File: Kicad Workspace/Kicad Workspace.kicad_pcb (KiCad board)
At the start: 2 copper layers, 105 parts, among them U2 PCM1863DBT, U4 TMUX1574PW, U6 TLV76733DRVx, U7 LM5017MR, U8 LT3042xMSE, U9 STM32G030C8Tx, Y1 Crystal

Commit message: project update
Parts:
- added J1: NMJ4HFD2, Connector_Audio:Jack_6.35mm_Neutrik_NMJ4HFD2_Horizontal, F.Cu at (235.5, 44.0)
- added J2: NMJ4HFD2, Connector_Audio:Jack_6.35mm_Neutrik_NMJ4HFD2_Horizontal, F.Cu at (235.5, 65.3)
- added J3: NMJ6HFD2, Connector_Audio:Jack_6.35mm_Neutrik_NMJ6HFD2_Horizontal, F.Cu at (235.5, 86.6)
- added J4: NMJ4HFD2, Connector_Audio:Jack_6.35mm_Neutrik_NMJ4HFD2_Horizontal, F.Cu at (235.5, 107.9)
- added U1: ~, FootPrints:FSC-BT1058, F.Cu at (64.0, 157.5)
- moved C22 24.3 mm to (129.3, 163.2)
- moved C23 24.3 mm to (129.3, 168.4)
- moved C13 24.3 mm to (121.8, 159.5)
- moved C14 24.3 mm to (123.8, 160.0)
- moved C15 24.3 mm to (123.8, 162.5)
- moved C16 24.3 mm to (121.8, 162.9)
- moved C19 24.3 mm to (121.8, 155.7)
- moved U2 24.3 mm to (135.5, 164.0)
- moved Y1 24.3 mm to (129.0, 165.8)
- moved C17 24.3 mm to (131.7, 169.2)
- moved C18 24.3 mm to (132.2, 171.1)
- moved U4 5.84 mm to (108.0, 46.5)

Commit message: feat: routing work in progress
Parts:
- added J5: L+, Connector_Wire:SolderWirePad_1x01_SMD_2x4mm, F.Cu at (201.5, 20.9)
- added J6: L-, Connector_Wire:SolderWirePad_1x01_SMD_2x4mm, F.Cu at (205.1, 20.9)
- added J7: R+, Connector_Wire:SolderWirePad_1x01_SMD_2x4mm, F.Cu at (208.6, 20.9)
- added J8: R-, Connector_Wire:SolderWirePad_1x01_SMD_2x4mm, F.Cu at (212.2, 20.9)
- added U3: PCM5242RHBT, FootPrints:PCM5242, F.Cu at (132.3, 105.3)
- added U5: TPA3255DDV, FootPrints:TPA3255, F.Cu at (201.5, 101.6)
- J3: value NMJ6HFD2 -> AudioJack3_Switch; footprint Connector_Audio:Jack_6.35mm_Neutrik_NMJ6HFD2_Horizontal -> Connector_Audio:Jack_3.5mm_CUI_SJ1-3535NG_Horizontal
- R11: footprint Resistor_SMD:R_01005_0402Metric -> Resistor_SMD:R_0201_0603Metric
- moved U6 212.2 mm to (265.0, 32.5)
- moved U7 212.2 mm to (260.1, 27.5)
- moved U8 212.2 mm to (259.5, 33.0)
- moved C59 200.0 mm to (267.6, 93.9)
- moved C60 200.0 mm to (267.6, 101.8)
- moved C61 200.0 mm to (267.6, 109.6)
- moved C62 200.0 mm to (267.6, 117.5)
- moved C63 200.0 mm to (237.4, 115.0)
- moved R14 200.0 mm to (274.5, 125.8)
- moved C65 200.0 mm to (252.4, 98.8)
- moved C66 200.0 mm to (252.4, 116.3)
- moved R15 200.0 mm to (271.1, 125.8)
- moved R16 200.0 mm to (271.1, 127.5)
- moved C33 200.0 mm to (266.1, 122.2)
- moved C38 200.0 mm to (266.1, 124.0)
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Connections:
- net /Amplification/L+ renamed Net-(J5-Pin_1)
- net /Amplification/L- renamed Net-(J6-Pin_1)
- net /Amplification/R+ renamed Net-(J7-Pin_1)
- net /Amplification/R- renamed Net-(J8-Pin_1)
- C10 pad 2: +3V3 -> +3.3V
- C28 pad 1: /Wired Input/MONO -> Net-(C28-Pad1)
- C30 pad 1: /Wired Input/MONO -> Net-(C28-Pad1)
- J4 pad S: unconnected-(J4-PadS) -> GND
- J4 pad T: unconnected-(J4-PadT) -> Net-(C28-Pad1)
- J4 pad TN: unconnected-(J4-PadTN) -> GND
- R9 pad 1: /Wired Input/MONO -> Net-(C28-Pad1)
- U1 pad 13: unconnected-(U1-BT_TX/PIO5-Pad13) -> /Bluetooth/UART.RX
- U1 pad 14: unconnected-(U1-BT_RX/PIO4-Pad14) -> /Bluetooth/UART.TX
- U1 pad 15: unconnected-(U1-BT_CTS/PIO3-Pad15) -> /Bluetooth/UART.RTS
- U1 pad 16: unconnected-(U1-BT_RTS/PIO2-Pad16) -> /Bluetooth/UART.CTS
- U1 pad 4: /Bluetooth/BT_BCK -> /Bluetooth/BT_I2S.BCK
- U1 pad 6: /Bluetooth/BT_DATA -> /Bluetooth/BT_I2S.DATA
- U1 pad 7: /Bluetooth/BT_LRCK -> /Bluetooth/BT_I2S.LRCK
- U2 pad 16: /Wired Input/WIRE_LRCK -> /EQ and DAC/WIRE_I2S.LRCK
- U2 pad 17: /Wired Input/WIRE_BCK -> /EQ and DAC/WIRE_I2S.BCK
- U2 pad 18: /Wired Input/WIRE_DATA -> /EQ and DAC/WIRE_I2S.DATA
- U2 pad 23: /Wired Input/SDA -> /EQ and DAC/I2C.SDA
- U2 pad 24: /Wired Input/SCL -> /EQ and DAC/I2C.SCL
- U4 pad 13: /EQ and DAC/WIRE_DATA -> /EQ and DAC/WIRE_I2S.DATA
- U4 pad 14: /EQ and DAC/BT_DATA -> /Bluetooth/BT_I2S.DATA
- U4 pad 16: +3V3 -> +3.3V
- U4 pad 2: /EQ and DAC/BT_LRCK -> /Bluetooth/BT_I2S.LRCK
- U4 pad 3: /EQ and DAC/WIRE_LRCK -> /EQ and DAC/WIRE_I2S.LRCK
- U4 pad 5: /EQ and DAC/BT_BCK -> /Bluetooth/BT_I2S.BCK
- U4 pad 6: /EQ and DAC/WIRE_BCK -> /EQ and DAC/WIRE_I2S.BCK
- U9 pad 29: /MCU/TX -> /Bluetooth/UART.TX
- U9 pad 32: /MCU/RX -> /Bluetooth/UART.RX
- U9 pad 33: /MCU/CTS -> /Bluetooth/UART.CTS
- U9 pad 34: /MCU/RTS -> /Bluetooth/UART.RTS
- U9 pad 45: /MCU/SCL -> /EQ and DAC/I2C.SCL
- U9 pad 46: /MCU/SDA -> /EQ and DAC/I2C.SDA
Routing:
- net +3.3VA: track 4.66 -> 0.08 mm

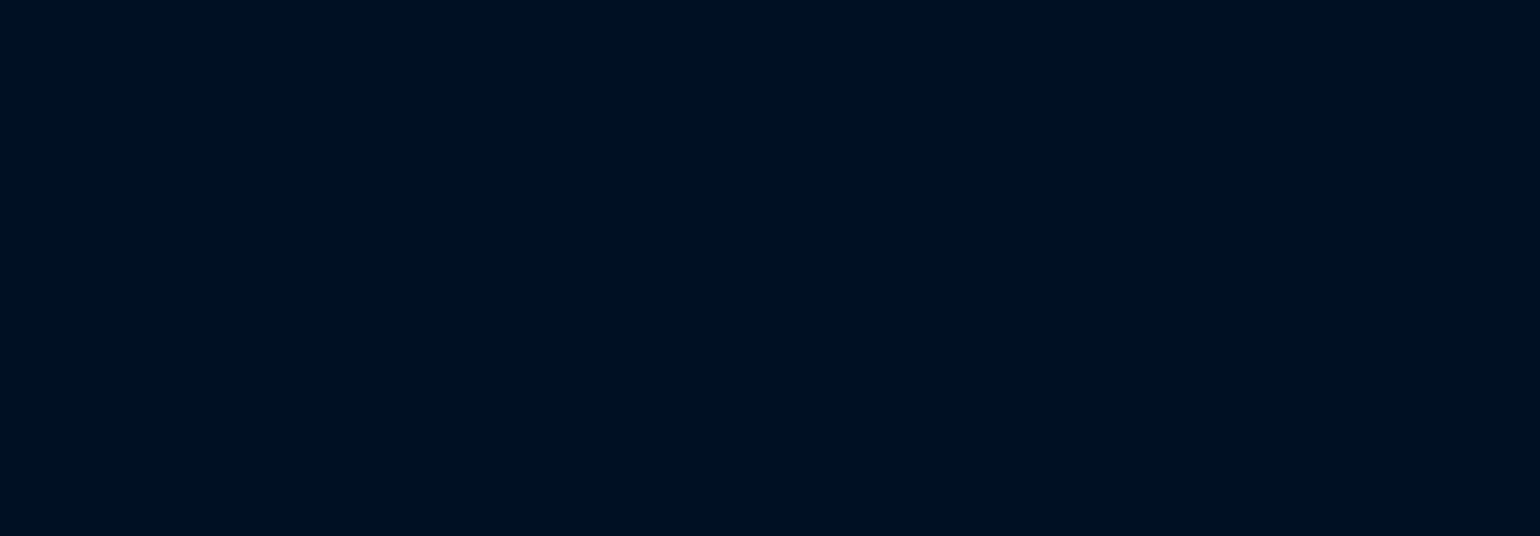
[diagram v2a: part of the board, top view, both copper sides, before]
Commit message: feat: routing work in progress
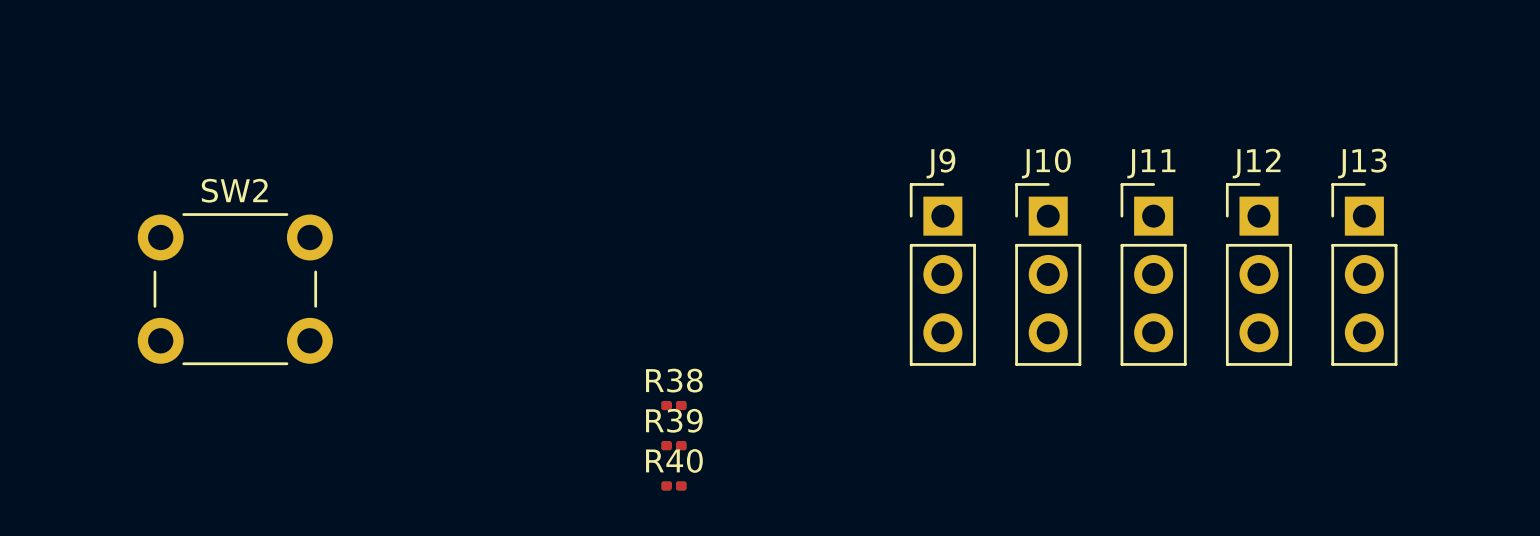
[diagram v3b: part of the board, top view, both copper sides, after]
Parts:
- added J10: Conn_01x03_Pin, Connector_PinHeader_2.54mm:PinHeader_1x03_P2.54mm_Vertical, F.Cu at (106.8, 175.5)
- added J11: Conn_01x03_Pin, Connector_PinHeader_2.54mm:PinHeader_1x03_P2.54mm_Vertical, F.Cu at (111.4, 175.5)
- added J12: Conn_01x03_Pin, Connector_PinHeader_2.54mm:PinHeader_1x03_P2.54mm_Vertical, F.Cu at (116.0, 175.5)
- added J13: Conn_01x03_Pin, Connector_PinHeader_2.54mm:PinHeader_1x03_P2.54mm_Vertical, F.Cu at (120.6, 175.5)
- added J9: Conn_01x03_Pin, Connector_PinHeader_2.54mm:PinHeader_1x03_P2.54mm_Vertical, F.Cu at (102.2, 175.5)
- added R38: 2.2K, Resistor_SMD:R_0201_0603Metric, F.Cu at (90.5, 183.7)
- added R39: 2.2K, Resistor_SMD:R_0201_0603Metric, F.Cu at (90.5, 185.5)
- added R40: 2.2K, Resistor_SMD:R_0201_0603Metric, F.Cu at (90.5, 187.2)
- added SW2: ~, Button_Switch_THT:SW_PUSH_6mm, F.Cu at (68.1, 176.4)
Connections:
- U9 pad 11: unconnected-(U9-Volume-Pad11) -> Net-(J9-Pin_2)
- U9 pad 12: unconnected-(U9-L/R-Pad12) -> Net-(J10-Pin_2)
- U9 pad 13: unconnected-(U9-EQ_low-Pad13) -> Net-(J11-Pin_2)
- U9 pad 14: unconnected-(U9-EQ_midle-Pad14) -> Net-(J12-Pin_2)
- U9 pad 15: unconnected-(U9-EQ_high-Pad15) -> Net-(J13-Pin_2)
- U9 pad 16: unconnected-(U9-Source-Pad16) -> Net-(U9-Source)
- U9 pad 48: unconnected-(U9-PAIR_BT-Pad48) -> Net-(U9-PAIR_BT)

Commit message: feat: routing TPA3255 output components placement
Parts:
- added L1: 10µH/25A, FootPrints:IND_SER2915L-103KL, F.Cu at (313.1, 54.8)
- added L2: 10µH/25A, FootPrints:IND_SER2915L-103KL, F.Cu at (185.1, 53.4)
- added L3: 10µH/25A, FootPrints:IND_SER2915L-103KL, F.Cu at (224.9, 53.3)
- added L4: 10µH/25A, FootPrints:IND_SER2915L-103KL, F.Cu at (268.7, 53.7)
- moved U8 175.2 mm to (269.2, 207.9)
- moved U6 175.2 mm to (274.7, 207.4)
- moved U7 175.2 mm to (269.8, 202.3)
- moved C51 124.5 mm to (327.3, 37.4)
- moved C48 123.3 mm to (334.4, 41.7), turned to 180 degrees
- moved J8 114.7 mm to (326.7, 26.3)
- moved C43 112.1 mm to (328.2, 69.7)
- moved C52 110.6 mm to (327.8, 32.5)
- moved R18 109.1 mm to (333.2, 32.7)
- moved C47 91.8 mm to (282.5, 35.6), turned to 180 degrees
- moved C49 77.6 mm to (282.4, 41.2)
- moved C33 77.0 mm to (254.3, 198.3)
- moved C38 77.0 mm to (254.3, 200.1)
- moved C39 77.0 mm to (254.3, 201.8)
- moved C41 77.0 mm to (261.6, 204.2)
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
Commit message: feat: routing work in progress
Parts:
- moved C66 150.0 mm to (265.4, 44.4), turned to 180 degrees
- moved C67 149.3 mm to (266.4, 58.5), turned to 180 degrees
- moved C68 147.5 mm to (266.3, 65.9), turned to 180 degrees
- moved C64 140.6 mm to (243.9, 57.1), turned to 180 degrees
- moved C65 131.1 mm to (243.6, 43.7), turned to 180 degrees
- moved C63 127.8 mm to (243.8, 64.5), turned to 180 degrees
- moved C42 110.9 mm to (257.8, 95.0), turned to 90 degrees
- moved C41 110.2 mm to (244.5, 95.2), turned to 90 degrees
- moved R16 109.8 mm to (258.2, 93.8)
- moved R15 108.8 mm to (244.2, 94.1), turned to 180 degrees
- moved C39 107.7 mm to (256.5, 94.1), turned to -90 degrees
- moved R13 107.0 mm to (250.0, 98.7), turned to -90 degrees
- moved U3 106.5 mm to (216.8, 170.2)
- moved C38 105.6 mm to (252.8, 94.5), turned to -90 degrees
- moved R14 104.2 mm to (247.8, 98.7), turned to -90 degrees
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
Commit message: feat: routing work in progress
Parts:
- added C71: 4.7µF, Capacitor_SMD:C_0805_2012Metric, F.Cu at (264.6, 227.7)
- added C72: 4.7µF, Capacitor_SMD:C_0805_2012Metric, F.Cu at (264.6, 230.7)
- added C73: 4.7µF, Capacitor_SMD:C_0805_2012Metric, F.Cu at (264.6, 233.8)
- added C74: 2.2µF, Capacitor_SMD:C_0201_0603Metric, F.Cu at (270.4, 227.1)
- added R21: 499, Resistor_SMD:R_0201_0603Metric, F.Cu at (270.4, 228.8)
- added R30: 33.2K/1%, Resistor_SMD:R_0805_2012Metric, F.Cu at (271.3, 232.9)
- added R31: 294K, Resistor_SMD:R_01005_0402Metric, F.Cu at (268.0, 227.1)
- added R32: 220K, Resistor_SMD:R_01005_0402Metric, F.Cu at (268.0, 228.7)
- added R33: 10K, Resistor_SMD:R_01005_0402Metric, F.Cu at (268.0, 230.3)
- added R34: 51.1K, Resistor_SMD:R_0201_0603Metric, F.Cu at (270.4, 230.6)
- added R35: 8.87K, Resistor_SMD:R_01005_0402Metric, F.Cu at (268.0, 232.0)
- added R36: 1K, Resistor_SMD:R_01005_0402Metric, F.Cu at (268.0, 233.7)
- C5: footprint Capacitor_SMD:C_0805_2012Metric -> Capacitor_SMD:C_0201_0603Metric
- moved C69 96.7 mm to (218.6, 180.4)
- moved C70 96.7 mm to (218.6, 182.2)
- moved R22 96.7 mm to (218.6, 183.9)
- moved R23 96.7 mm to (218.6, 185.7)
- moved R24 96.7 mm to (218.6, 187.4)
- moved R25 96.7 mm to (208.2, 183.3)
- moved R26 96.7 mm to (208.2, 185.0)
- moved R27 96.7 mm to (208.2, 186.8)
- moved R28 96.7 mm to (208.2, 188.5)
- moved R29 96.7 mm to (208.2, 190.3)
- moved C9 87.1 mm to (214.0, 174.1), turned to 180 degrees
- moved C8 87.0 mm to (213.4, 172.3), turned to 180 degrees
- moved C2 86.9 mm to (205.3, 170.1), turned to 90 degrees
- moved C6 84.9 mm to (208.4, 173.7), turned to 180 degrees
- moved C1 83.9 mm to (207.1, 169.1), turned to 90 degrees
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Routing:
- net +3.3V: track 3.74 -> 13.0 mm
- net Net-(U2-LDO): track 4.64 -> 12.5 mm
- net /Wired Input/VIN2_R: track 0.00 -> 7.74 mm
- net /Wired Input/VIN1_L: track 0.00 -> 6.09 mm
- net /Wired Input/VIN1_R: track 0.00 -> 5.27 mm
- net /Wired Input/VIN2_L: track 0.00 -> 4.11 mm
- net Net-(U2-VREF): track 6.81 -> 10.9 mm
- net Net-(C28-Pad1): track 0.00 -> 3.83 mm
- net /Wired Input/VIN3_R: track 0.00 -> 3.62 mm
- net /Wired Input/VIN3_L: track 0.00 -> 3.43 mm
- net Net-(U3-VNEG): track 0.00 -> 2.98 mm
- net Net-(U3-LDOO): track 0.00 -> 2.97 mm
- net Net-(C26-Pad2): track 0.00 -> 1.92 mm
- net Net-(C11-Pad1): track 0.00 -> 1.82 mm
- net Net-(C24-Pad2): track 0.00 -> 1.81 mm
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- added copper zone on F.Cu, net +3.3V
